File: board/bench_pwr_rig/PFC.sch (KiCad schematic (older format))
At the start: 32 parts

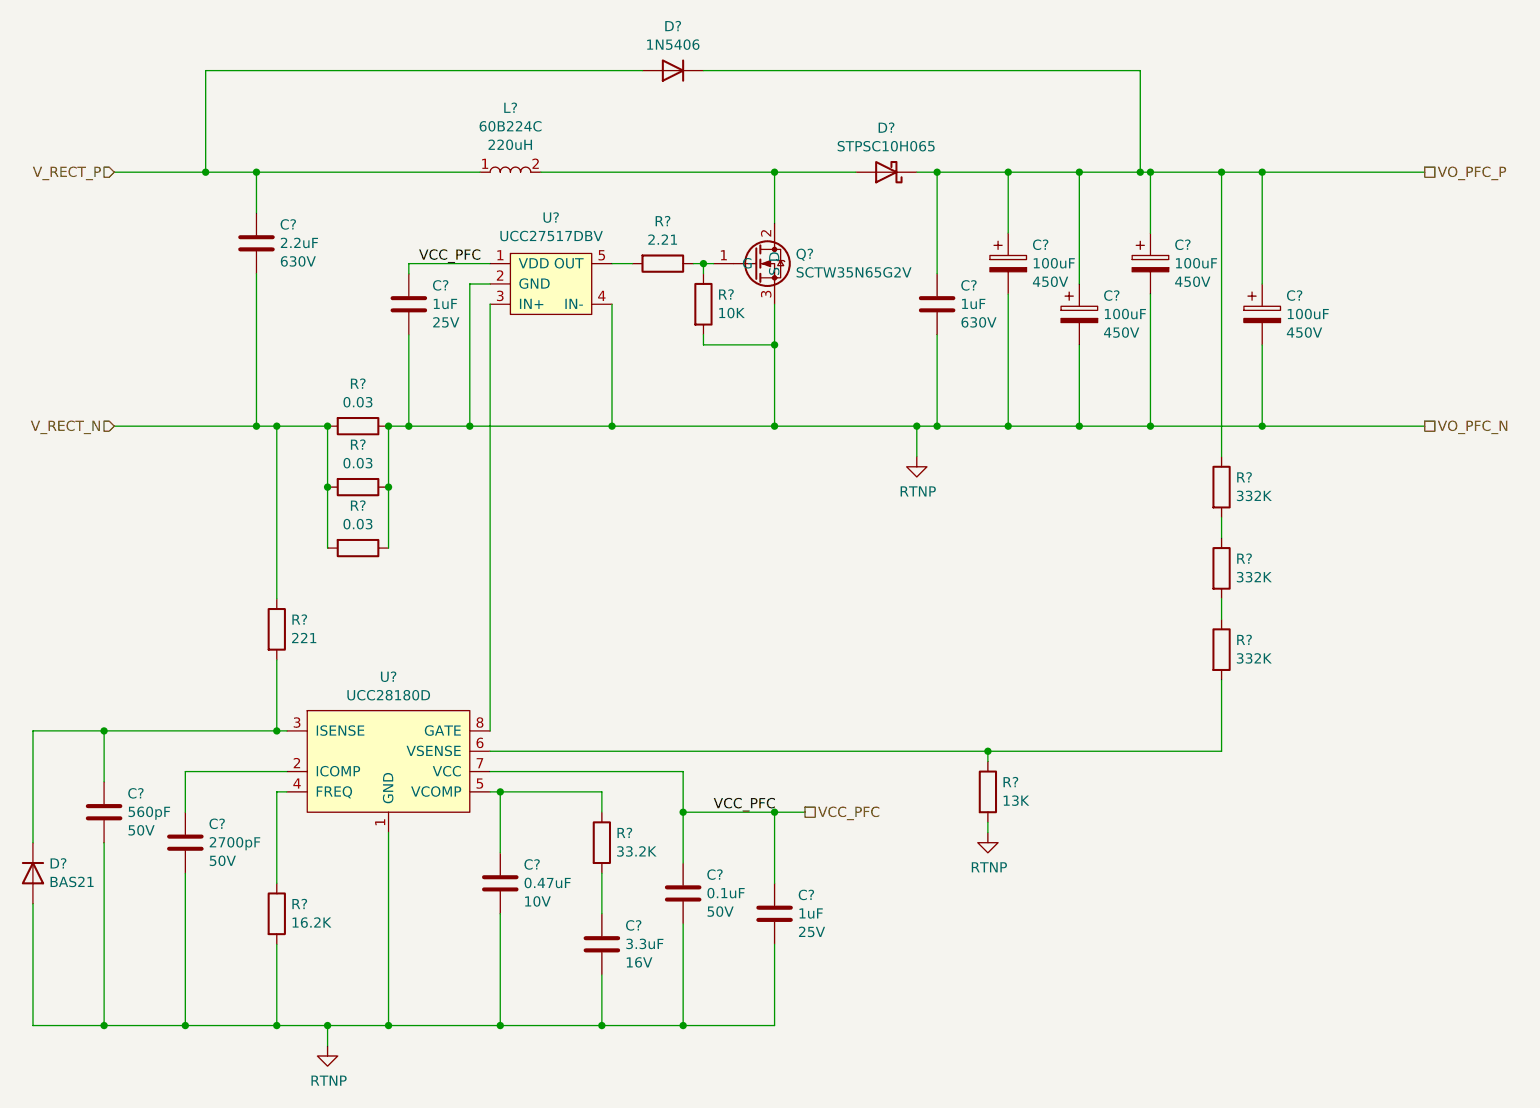
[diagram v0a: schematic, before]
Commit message: schematic and layout updates
Finalized schematic for rev 0.1. Anticipate additional component values update through analysis. Moving to layout
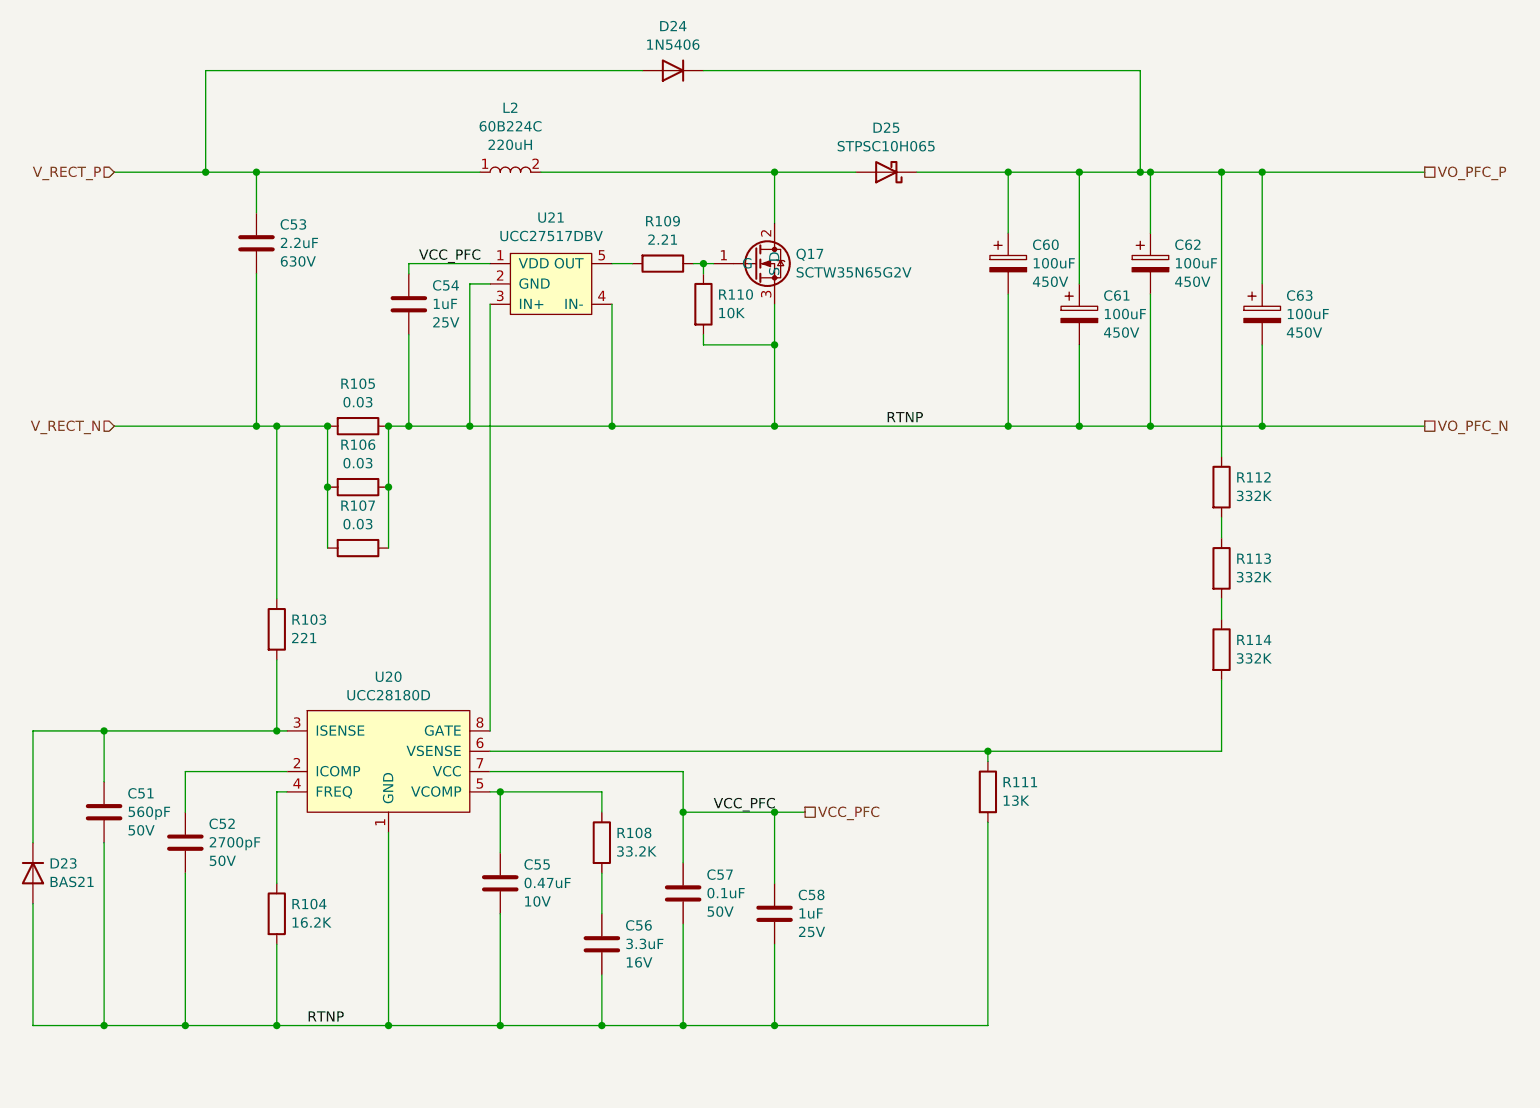
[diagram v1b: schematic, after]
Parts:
- removed C?: R75PR4100AA30K, Capacitor_THT:C_Rect_L33.0mm_W13.0mm_P27.50mm_MKS4, symbol Capacitor:R75PR4100AA30K
- gave numbers to parts that had none: 31
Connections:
- net GND renamed VO_PFC_N

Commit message: Updated layout
Added output screw terminal
Added mounting screws M4
Changed primary ground to secondary ground plane coupling capacitor to radial disc type with safety rating X1, Y1
Continued layout
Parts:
- removed C57: C1608X7R1H104K, Capacitor_SMD:C_0603_1608Metric_Pad1.05x0.95mm_HandSolder, symbol Capacitor:C1608X7R1H104K
- removed C58: C1608X7R1E105K080AB, Capacitor_SMD:C_0603_1608Metric_Pad1.05x0.95mm_HandSolder, symbol Capacitor:C1608X7R1E105K080AB
- added C57: CC0805KRX7R9BB104, Capacitor_SMD:C_0805_2012Metric_Pad1.15x1.40mm_HandSolder, symbol Capacitor:CC0805KRX7R9BB104
- added C58: CL21B105KBFNNNE, Capacitor_SMD:C_0805_2012Metric_Pad1.15x1.40mm_HandSolder, symbol Capacitor:CL21B105KBFNNNE
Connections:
- net VCC_PFC: now also C57.1, C58.1
- net VO_PFC_N: now also C57.2, C58.2
- net BST-SW-NODE: now reaches D25.2 (A), L2.2, Q17.2 (D)
- net U20-OUT: now reaches U20.8 (GATE), U21.3 (IN+)
- net U20-ICOMP: now reaches C52.1, U20.2 (ICOMP)
- net U20-ISNS: now reaches C51.1, D23.3 (K), R103.2, U20.3 (ISENSE)
- net BST-FREQ: now reaches R104.1, U20.4 (FREQ)
- net BST-VCMP: now reaches C55.1, R108.1, U20.5 (VCOMP)
- net BST-VSNS: now reaches R111.1, R114.2, U20.6 (VSENSE)
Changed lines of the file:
@@
-$EndComp
-$Comp
-L Capacitor:C1608X7R1E105K080AB C58
-U 1 1 605CB970
-P 7450 5350
-F 0 "C58" H 7565 5441 50  0000 L CNN
-F 1 "C1608X7R1E105K080AB" H 8000 5150 50  0001 C CNN
-F 2 "Capacitor_SMD:C_0603_1608Metric_Pad1.05x0.95mm_HandSolder" H 7450 5350 50  0001 C CNN
-F 3 "https://content.kemet.com/datasheets/KEM_C1064_X1_400_VAC_Y2_250_VAC.pdf" H 7450 5350 50  0001 C CNN
-F 4 "1uF" H 7565 5350 50  0000 L CNN "Capacitance"
-F 5 "25V" H 7565 5259 50  0000 L CNN "Voltage"
-	1    7450 5350
-	1    0    0    -1
-$EndComp
-$Comp
-L Capacitor:C1608X7R1H104K C57
-U 1 1 605D6D7F
-P 7000 5250
-F 0 "C57" H 7115 5341 50  0000 L CNN
-F 1 "C1608X7R1H104K" H 7550 5050 50  0001 C CNN
-F 2 "Capacitor_SMD:C_0603_1608Metric_Pad1.05x0.95mm_HandSolder" H 7000 5250 50  0001 C CNN
-F 3 "https://content.kemet.com/datasheets/KEM_C1064_X1_400_VAC_Y2_250_VAC.pdf" H 7000 5250 50  0001 C CNN
-F 4 "0.1uF" H 7115 5250 50  0000 L CNN "Capacitance"
-F 5 "50V" H 7115 5159 50  0000 L CNN "Voltage"
-	1    7000 5250
-	1    0    0    -1
 $EndComp
 $Comp
@@
 Text Label 5150 5900 0    50   ~ 0
 RTNP
+Text Label 7100 1700 0    50   ~ 0
+BST-SW-NODE
+Text Label 4550 4650 0    50   ~ 0
+U20-ICOMP
+Text Label 4300 4450 0    50   ~ 0
+U20-ISNS
+Text Label 6050 4200 1    50   ~ 0
+U20-OUT
+Text Label 6350 4550 0    50   ~ 0
+BST-VSNS
+Text Label 6200 4750 0    50   ~ 0
+BST-VCMP
+Text Label 5000 5150 1    50   ~ 0
+BST-FREQ
+$Comp
+L Capacitor:CC0805KRX7R9BB104 C57
+U 1 1 5FB4849D
+P 7000 5250
+F 0 "C57" H 7115 5341 50  0000 L CNN
+F 1 "CC0805KRX7R9BB104" H 7550 5050 50  0001 C CNN
+F 2 "Capacitor_SMD:C_0805_2012Metric_Pad1.15x1.40mm_HandSolder" H 7000 5250 50  0001 C CNN
+F 3 "https://datasheet.lcsc.com/szlcsc/Samsung-Electro-Mechanics-CL21B103KCANNNC_C18741.pdf" H 7000 5250 50  0001 C CNN
+F 4 "0.1uF" H 7115 5250 50  0000 L CNN "Capacitance"
+F 5 "50V" H 7115 5159 50  0000 L CNN "Voltage"
+	1    7000 5250
+	1    0    0    -1
+$EndComp
+$Comp
+L Capacitor:CL21B105KBFNNNE C58
+U 1 1 5FB48B3E
+P 7450 5350
+F 0 "C58" H 7565 5441 50  0000 L CNN
+F 1 "CL21B105KBFNNNE" H 8000 5150 50  0001 C CNN
+F 2 "Capacitor_SMD:C_0805_2012Metric_Pad1.15x1.40mm_HandSolder" H 7450 5350 50  0001 C CNN
+F 3 "https://datasheet.lcsc.com/szlcsc/Samsung-Electro-Mechanics-CL21B103KCANNNC_C18741.pdf" H 7450 5350 50  0001 C CNN
+F 4 "1uF" H 7565 5350 50  0000 L CNN "Capacitance"
+F 5 "50V" H 7565 5259 50  0000 L CNN "Voltage"
+	1    7450 5350
+	1    0    0    -1
+$EndComp
 $EndSCHEMATC
